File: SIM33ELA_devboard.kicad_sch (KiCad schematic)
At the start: 10 parts, among them J2 Conn_01x13_Pin, U2 SIM33ELA

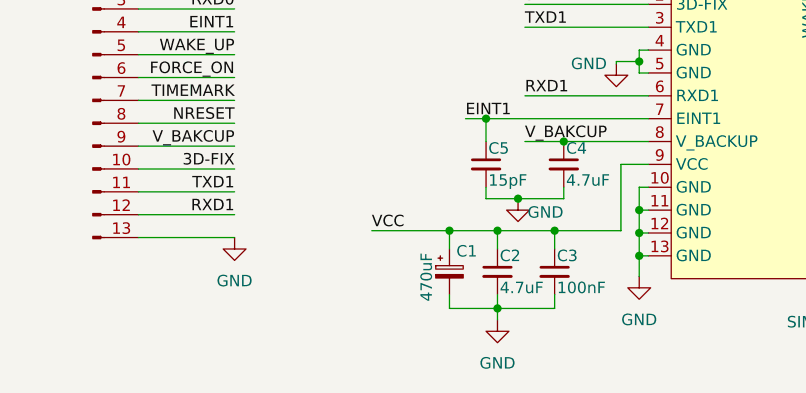
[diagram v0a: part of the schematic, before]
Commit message: RF modificado, agregado led de POWER
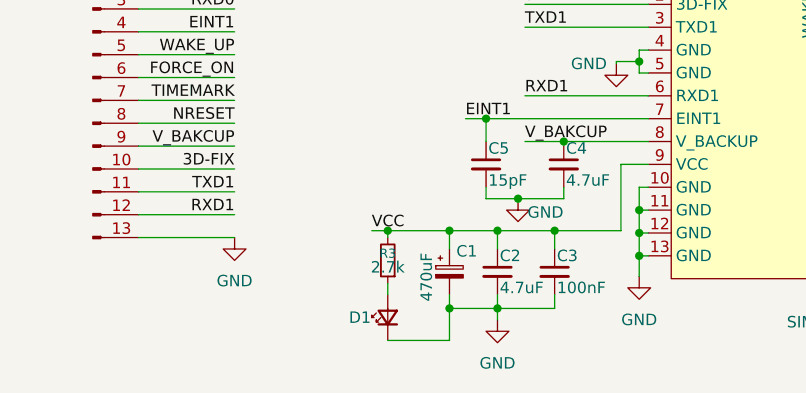
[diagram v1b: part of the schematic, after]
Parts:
- added D1: LED_Small, LED_SMD:LED_0603_1608Metric_Pad1.05x0.95mm_HandSolder, symbol Device:LED_Small
- added R3: 2.7k, Resistor_SMD:R_0603_1608Metric, symbol Device:R_Small
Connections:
- net GND: now also D1.1 (K)
- net VCC: now also R3.2
- new net: D1.2 (A), R3.1
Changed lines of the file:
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@@
+	)
+	(junction
+		(at 114.3 115.57)
+		(diameter 0)
+		(color 0 0 0 0)
 	)
 	(junction
@@
 	)
 	(junction
+		(at 121.158 124.206)
+		(diameter 0)
+		(color 0 0 0 0)
+	)
+	(junction
 		(at 132.842 115.57)
 		(diameter 0)
@@
 	(wire
 		(pts
+			(xy 114.3 127.762) (xy 121.158 127.762)
+		)
+		(stroke
+			(width 0)
+			(type default)
+		)
+	)
+	(wire
+		(pts
 			(xy 187.706 106.934) (xy 183.642 106.934)
 		)
@@
 	(wire
 		(pts
-			(xy 112.522 115.57) (xy 121.158 115.57)
+			(xy 112.522 115.57) (xy 114.3 115.57)
 		)
 		(stroke
@@
 	(wire
 		(pts
+			(xy 114.3 115.57) (xy 114.3 116.332)
+		)
+		(stroke
+			(width 0)
+			(type default)
+		)
+	)
+	(wire
+		(pts
 			(xy 158.496 82.804) (xy 158.496 78.994)
 		)
@@
 	(wire
 		(pts
+			(xy 121.158 127.762) (xy 121.158 124.206)
+		)
+		(stroke
+			(width 0)
+			(type default)
+		)
+	)
+	(wire
+		(pts
 			(xy 129.54 90.424) (xy 143.256 90.424)
 		)
@@
 	(wire
 		(pts
+			(xy 114.3 121.412) (xy 114.3 122.682)
+		)
+		(stroke
+			(width 0)
+			(type default)
+		)
+	)
+	(wire
+		(pts
 			(xy 86.614 116.332) (xy 97.282 116.332)
 		)
@@
 		(pts
 			(xy 125.222 112.014) (xy 125.222 110.744)
+		)
+		(stroke
+			(width 0)
+			(type default)
+		)
+	)
+	(wire
+		(pts
+			(xy 114.3 115.57) (xy 121.158 115.57)
 		)
 		(stroke
@@
 					(unit 1)
 				)
+			)
+		)
+	)
+	(symbol
+		(lib_id "Device:R_Small")
+		(at 114.3 118.872 180)
+		(unit 1)
+		(exclude_from_sim no)
+		(in_bom yes)
+		(on_board yes)
+		(dnp no)
+		(property "Reference" "R3"
+			(at 114.3 118.11 0)
+			(effects
+				(font
+					(size 1.016 1.016)
+				)
+			)
+		)
+		(property "Value" "2.7k"
+			(at 114.3 119.634 0)
+			(effects
+				(font
+					(size 1.27 1.27)
+				)
+			)
+		)
+		(property "Footprint" "Resistor_SMD:R_0603_1608Metric"
+			(at 114.3 118.872 0)
+			(effects
+				(font
+					(size 1.27 1.27)
+				)
+				(hide yes)
+			)
+		)
+		(property "Datasheet" "~"
+			(at 114.3 118.872 0)
+			(effects
+				(font
+					(size 1.27 1.27)
+				)
+				(hide yes)
+			)
+		)
+		(property "Description" "Resistor, small symbol"
+			(at 114.3 118.872 0)
+			(effects
+				(font
+					(size 1.27 1.27)
+				)
+				(hide yes)
+			)
+		)
+		(pin "1"
+		)
+		(pin "2"
+		)
+		(instances
+			(project "SIM33ELA_devboard"
+				(path "/f319b420-bec3-402d-8d90-88207d1d0c16"
+					(reference "R3")
+					(unit 1)
+				)
+			)
+		)
+	)
+	(symbol
+		(lib_id "Device:LED_Small")
+		(at 114.3 125.222 90)
+		(unit 1)
+		(exclude_from_sim no)
+		(in_bom yes)
+		(on_board yes)
+		(dnp no)
+		(property "Reference" "D1"
+			(at 109.982 125.222 90)
+			(effects
+				(font
+					(size 1.27 1.27)
+				)
+				(justify right)
+			)
+		)
+		(property "Value" "LED_Small"
+			(at 116.84 126.4284 90)
+			(effects
+				(font
+					(size 1.27 1.27)
+				)
+				(justify right)
+				(hide yes)
+			)
+		)
+		(property "Footprint" "LED_SMD:LED_0603_1608Metric_Pad1.05x0.95mm_HandSolder"
+			(at 114.3 125.222 90)
+			(effects
+				(font
+					(size 1.27 1.27)
+				)
+				(hide yes)
+			)
+		)
+		(property "Datasheet" "~"
+			(at 114.3 125.222 90)
+			(effects
+				(font
+					(size 1.27 1.27)
+				)
+				(hide yes)
+			)
+		)
+		(property "Description" "Light emitting diode, small symbol"
+			(at 114.3 125.222 0)
+			(effects
+				(font
+					(size 1.27 1.27)
+				)
+				(hide yes)
+			)
+		)
+		(property "Sim.Pin" "1=K 2=A"
+			(at 114.3 125.222 0)
+			(effects
+				(font
+					(size 1.27 1.27)
+				)
+				(hide yes)
+			)
+		)
+		(pin "2"
+		)
+		(pin "1"
+		)
+		(instances
+			(project ""
+				(path "/f319b420-bec3-402d-8d90-88207d1d0c16"
+					(reference "D1")
+					(unit 1)
+				)

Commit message: por si acaso
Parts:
- R3: value 2.7k -> 4.7k
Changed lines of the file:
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@@
 			)
 		)
-		(property "Value" "2.7k"
+		(property "Value" "4.7k"
 			(at 114.3 119.634 0)
 			(effects

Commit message: cambios finales
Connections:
- net RF_SIGNAL1: now reaches U2.16 (ANT), U2.17 (RF_IN)
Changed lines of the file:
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@@
+	(wire
+		(pts
+			(xy 183.642 110.744) (xy 183.642 113.284)
+		)
+		(stroke
+			(width 0)
+			(type default)
+		)
+	)
+	(wire
+		(pts
+			(xy 183.642 113.284) (xy 182.626 113.284)
+		)
+		(stroke
+			(width 0)
+			(type default)
+		)
+	)
 	(wire
 		(pts
@@
 	(wire
 		(pts
-			(xy 187.706 110.49) (xy 187.706 106.934)
+			(xy 187.706 108.458) (xy 187.706 106.934)
 		)
 		(stroke
@@
 	(wire
 		(pts
-			(xy 183.642 110.744) (xy 183.642 113.284)
-		)
-		(stroke
-			(width 0)
-			(type default)
-		)
-	)
-	(wire
-		(pts
 			(xy 183.642 115.824) (xy 183.642 118.364)
 		)
@@
 		(pts
 			(xy 142.24 113.284) (xy 143.256 113.284)
-		)
-		(stroke
-			(width 0)
-			(type default)
-		)
-	)
-	(wire
-		(pts
-			(xy 183.642 113.284) (xy 182.626 113.284)
 		)
 		(stroke
@@
 			(font
 				(size 1.27 1.27)
+			)
+			(justify left bottom)
+		)
+	)
+	(label "RF_SIGNAL1"
+		(at 183.642 113.284 0)
+		(effects
+			(font
+				(size 0.508 0.508)
 			)
 			(justify left bottom)
@@
 	(symbol
 		(lib_id "power:GND")
-		(at 187.706 110.49 0)
+		(at 187.706 108.458 0)
 		(unit 1)
 		(exclude_from_sim no)
@@
 		(on_board yes)
 		(dnp no)
-		(fields_autoplaced yes)
 		(property "Reference" "#PWR03"
-			(at 187.706 116.84 0)
+			(at 187.706 114.808 0)
 			(effects
 				(font
@@
 		)
 		(property "Value" "GND"
-			(at 187.706 115.316 0)
+			(at 191.008 110.236 0)
 			(effects
 				(font
@@
 		)
 		(property "Footprint" ""
-			(at 187.706 110.49 0)
+			(at 187.706 108.458 0)
 			(effects
 				(font
@@
 		)
 		(property "Datasheet" ""
-			(at 187.706 110.49 0)
+			(at 187.706 108.458 0)
 			(effects
 				(font
@@
 		)
 		(property "Description" "Power symbol creates a global label with name \"GND\" , ground"
-			(at 187.706 110.49 0)
-			(effects
-				(font
+			(at 187.706 108.458 0)
+			(effects
+				(font

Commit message: aaa
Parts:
- removed C1: 470uF, Capacitor_SMD:CP_Elec_6.3x7.7, symbol Device:C_Polarized_Small
- removed J2: Conn_01x13_Pin, Connector_PinHeader_2.54mm:PinHeader_1x13_P2.54mm_Vertical, symbol Connector:Conn_01x13_Pin
- added J1: Conn_01x14_Pin, Connector_PinHeader_2.54mm:PinHeader_1x14_P2.54mm_Vertical, symbol Connector:Conn_01x14_Pin
- added JP1: SolderJumper_2_Open, Jumper:SolderJumper-2_P1.3mm_Open_RoundedPad1.0x1.5mm, symbol Jumper:SolderJumper_2_Open
- added U1: XC6206P332MR, EasyEDA:SOT-23-3_L2.9-W1.6-P1.90-LS2.8-BR, symbol EasyEDA:XC6206P332MR
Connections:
- net 3D-FIX: now also J1.11 (Pin_11)
- net EINT1: now also J1.5 (Pin_5)
- net FORCE_ON: now also J1.7 (Pin_7)
- net GND: now also J1.14 (Pin_14), U1.1 (GND)
- net NRESET: now also J1.9 (Pin_9)
- net RXD0: now also J1.4 (Pin_4)
- net RXD1: now also J1.13 (Pin_13)
- net TIMEMARK: now also J1.8 (Pin_8)
- net TXD0: now also J1.3 (Pin_3)
- net TXD1: now also J1.12 (Pin_12)
- net VCC: now also J1.2 (Pin_2), JP1.2 (B), U1.2 (Vout); no longer R3.2
- net V_BAKCUP: now also J1.10 (Pin_10)
- net WAKE_UP: now also J1.6 (Pin_6)
- new net: JP1.1 (A), R3.2
- new net LDO: J1.1 (Pin_1), U1.3 (Vin)
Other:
- moved on the sheet: D1, R3
